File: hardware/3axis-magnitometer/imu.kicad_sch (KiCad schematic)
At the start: 3 parts, among them U9 LSM6DS3

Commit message: начата новая трассировка
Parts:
- renumbered C32 to C35, C33 to C36, U9 to U11
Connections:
- net INT1: no longer names the net of U11.4 (INT1)
- net INT2: no longer names the net of U11.9 (INT2)
- no-connect marks 2 -> 4
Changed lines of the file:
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@@
 		(at 144.78 82.55)
 	)
+	(no_connect
+		(at 195.58 80.01)
+	)
+	(no_connect
+		(at 195.58 77.47)
+	)
 	(wire
 		(pts
@@
 			(width 0)
 			(type default)
-		)
-	)
-	(hierarchical_label "INT1"
-		(shape output)
-		(at 195.58 77.47 0)
-		(effects
-			(font
-				(size 1.27 1.27)
-			)
-			(justify left)
-		)
-	)
-	(hierarchical_label "INT2"
-		(shape output)
-		(at 195.58 80.01 0)
-		(effects
-			(font
-				(size 1.27 1.27)
-			)
-			(justify left)
 		)
 	)
@@
 		(on_board yes)
 		(dnp no)
-		(property "Reference" "C32"
+		(property "Reference" "C35"
 			(at 175.514 95.25 90)
 			(effects
@@
 			(project "3axis-magnitometer"
 				(path "/c590c88d-27c9-4e5a-a435-a42d9de70c1c/be6038e0-c8de-46ff-af13-cf0ae52994ef"
-					(reference "C32")
+					(reference "C35")
 					(unit 1)
 				)
@@
 		(on_board yes)
 		(dnp no)
-		(property "Reference" "C33"
+		(property "Reference" "C36"
 			(at 185.674 95.25 90)
 			(effects
@@
 			(project "3axis-magnitometer"
 				(path "/c590c88d-27c9-4e5a-a435-a42d9de70c1c/be6038e0-c8de-46ff-af13-cf0ae52994ef"
-					(reference "C33")
+					(reference "C36")
 					(unit 1)
 				)
@@
 		(dnp no)
 		(fields_autoplaced yes)
-		(property "Reference" "U9"
+		(property "Reference" "U11"
 			(at 162.1633 100.33 0)
 			(effects
@@
 			(project ""
 				(path "/c590c88d-27c9-4e5a-a435-a42d9de70c1c/be6038e0-c8de-46ff-af13-cf0ae52994ef"
-					(reference "U9")
+					(reference "U11")
 					(unit 1)
 				)

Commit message: трасировка магнитометра
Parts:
- added C37: 0.22, Capacitor_SMD:C_0805_2012Metric, symbol Device:C
- added FB3, FB4: FerriteBead, Inductor_SMD:L_0805_2012Metric, symbol Device:FerriteBead
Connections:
- net GND: now also C37.1
- net VDA: now also FB4.2; no longer C35.2, U11.8 (VDD)
- net VDD: now also FB3.2; no longer C36.2, U11.12 (CS), U11.5 (VDDIO)
- new net: C35.2, FB4.1, U11.8 (VDD)
- new net: C36.2, C37.2, FB3.1, U11.12 (CS), U11.5 (VDDIO)

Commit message: Финальные правки трассировки
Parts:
- renumbered C35 to C36, C36 to C37, C37 to C38
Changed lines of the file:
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@@
 		(on_board yes)
 		(dnp no)
-		(property "Reference" "C35"
+		(property "Reference" "C36"
 			(at 175.514 95.25 90)
 			(effects
@@
 			(project "3axis-magnitometer"
 				(path "/c590c88d-27c9-4e5a-a435-a42d9de70c1c/be6038e0-c8de-46ff-af13-cf0ae52994ef"
-					(reference "C35")
+					(reference "C36")
 					(unit 1)
 				)
@@
 		(on_board yes)
 		(dnp no)
-		(property "Reference" "C36"
+		(property "Reference" "C37"
 			(at 185.674 95.25 90)
 			(effects
@@
 			(project "3axis-magnitometer"
 				(path "/c590c88d-27c9-4e5a-a435-a42d9de70c1c/be6038e0-c8de-46ff-af13-cf0ae52994ef"
-					(reference "C36")
+					(reference "C37")
 					(unit 1)
 				)
@@
 		(on_board yes)
 		(dnp no)
-		(property "Reference" "C37"
+		(property "Reference" "C38"
 			(at 194.564 95.25 90)
 			(effects
@@
 			(project "3axis-magnitometer"
 				(path "/c590c88d-27c9-4e5a-a435-a42d9de70c1c/be6038e0-c8de-46ff-af13-cf0ae52994ef"
-					(reference "C37")
+					(reference "C38")
 					(unit 1)
 				)

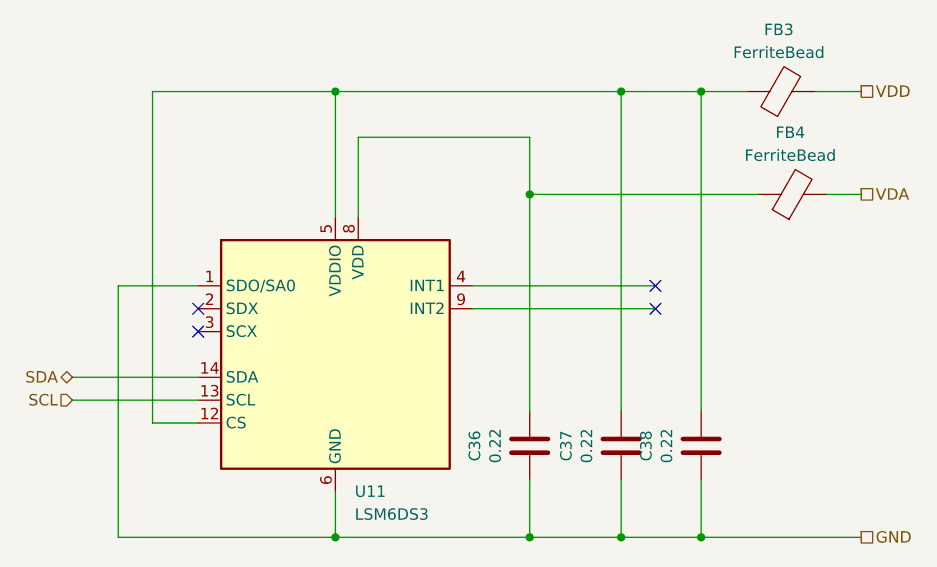
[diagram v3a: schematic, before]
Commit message: замена микросхемы преобразователя  уровня
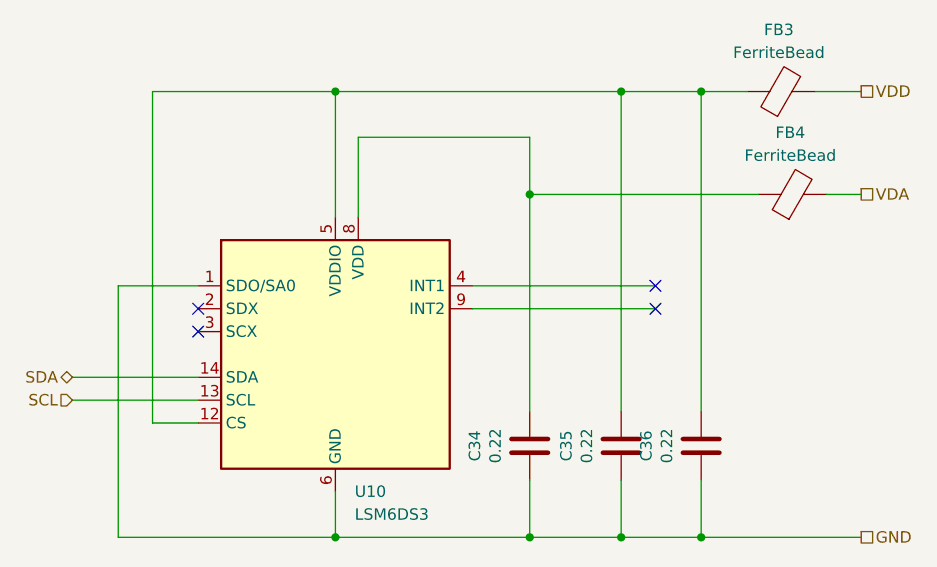
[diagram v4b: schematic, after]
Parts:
- renumbered C36 to C34, C37 to C35, C38 to C36, U11 to U10
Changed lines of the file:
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@@
 		(on_board yes)
 		(dnp no)
-		(property "Reference" "C36"
+		(property "Reference" "C34"
 			(at 175.514 95.25 90)
 			(effects
@@
 			(project "3axis-magnitometer"
 				(path "/c590c88d-27c9-4e5a-a435-a42d9de70c1c/be6038e0-c8de-46ff-af13-cf0ae52994ef"
-					(reference "C36")
+					(reference "C34")
 					(unit 1)
 				)
@@
 		(on_board yes)
 		(dnp no)
-		(property "Reference" "C37"
+		(property "Reference" "C35"
 			(at 185.674 95.25 90)
 			(effects
@@
 			(project "3axis-magnitometer"
 				(path "/c590c88d-27c9-4e5a-a435-a42d9de70c1c/be6038e0-c8de-46ff-af13-cf0ae52994ef"
-					(reference "C37")
+					(reference "C35")
 					(unit 1)
 				)
@@
 		(on_board yes)
 		(dnp no)
-		(property "Reference" "C38"
+		(property "Reference" "C36"
 			(at 194.564 95.25 90)
 			(effects
@@
 			(project "3axis-magnitometer"
 				(path "/c590c88d-27c9-4e5a-a435-a42d9de70c1c/be6038e0-c8de-46ff-af13-cf0ae52994ef"
-					(reference "C38")
+					(reference "C36")
 					(unit 1)
 				)
@@
 		(dnp no)
 		(fields_autoplaced yes)
-		(property "Reference" "U11"
+		(property "Reference" "U10"
 			(at 162.1633 100.33 0)
 			(effects
@@
 			(project ""
 				(path "/c590c88d-27c9-4e5a-a435-a42d9de70c1c/be6038e0-c8de-46ff-af13-cf0ae52994ef"
-					(reference "U11")
-					(unit 1)
-				)
+					(reference "U10")
+					(unit 1)
+				)
